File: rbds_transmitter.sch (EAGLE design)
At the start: 62 parts, among them IC1 MAX1551, IC2 TPS61030, IC3 MCP4812, IC4 OPA4743UA, Q1 P-Ch, SW1 FSMSM, U3 ATMEGA328, X1 HD44780LCD-1602, Y1 16Mhz

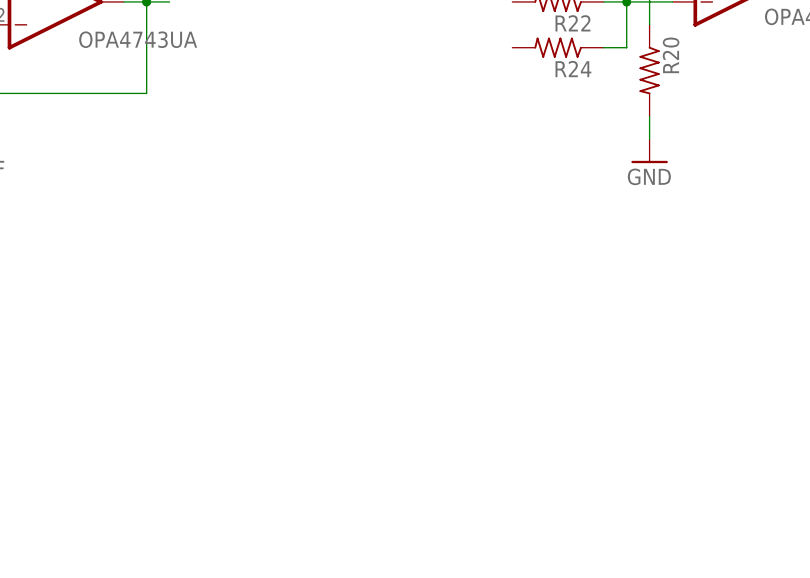
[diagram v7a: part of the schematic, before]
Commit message: adding low pass for pilot tones
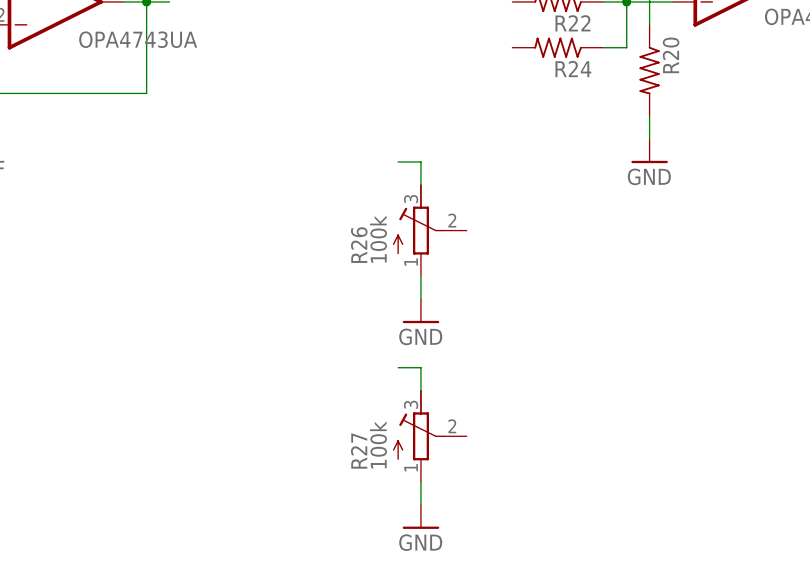
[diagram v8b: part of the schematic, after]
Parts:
- added R26, R27: 100k, rcl:R-TRIMM4G/J
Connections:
- new net N$32: R27.E
- new net N$33: R26.E
- net GND: now also R26.A, R27.A
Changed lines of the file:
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@@
 <part name="GND27" library="sparkfun" deviceset="GND" device=""/>
 <part name="C13" library="adafruit" deviceset="C-US" device="C1206" value="3.8nF"/>
+<part name="R26" library="rcl" deviceset="R-TRIMM" device="4G/J" value="100k"/>
+<part name="R27" library="rcl" deviceset="R-TRIMM" device="4G/J" value="100k"/>
+<part name="GND29" library="sparkfun" deviceset="GND" device=""/>
+<part name="GND30" library="sparkfun" deviceset="GND" device=""/>
 </parts>
 <sheets>
@@
 <instance part="GND27" gate="1" x="330.2" y="-60.96"/>
 <instance part="C13" gate="G$1" x="320.04" y="-22.86" rot="R90"/>
+<instance part="R26" gate="G$1" x="383.54" y="-58.42"/>
+<instance part="R27" gate="G$1" x="383.54" y="-81.28"/>
+<instance part="GND29" gate="1" x="383.54" y="-91.44"/>
+<instance part="GND30" gate="1" x="383.54" y="-68.58"/>
 </instances>
 <busses>
@@
 <pinref part="GND27" gate="1" pin="GND"/>
 <wire x1="330.2" y1="-58.42" x2="330.2" y2="-53.34" width="0.1524" layer="91"/>
+</segment>
+<segment>
+<pinref part="GND30" gate="1" pin="GND"/>
+<pinref part="R26" gate="G$1" pin="A"/>
+<wire x1="383.54" y1="-63.5" x2="383.54" y2="-66.04" width="0.1524" layer="91"/>
+</segment>
+<segment>
+<pinref part="GND29" gate="1" pin="GND"/>
+<pinref part="R27" gate="G$1" pin="A"/>
+<wire x1="383.54" y1="-86.36" x2="383.54" y2="-88.9" width="0.1524" layer="91"/>
 </segment>
 </net>
@@
 </segment>
 </net>
+<net name="N$32" class="0">
+<segment>
+<pinref part="R27" gate="G$1" pin="E"/>
+<wire x1="383.54" y1="-76.2" x2="383.54" y2="-73.66" width="0.1524" layer="91"/>
+<wire x1="383.54" y1="-73.66" x2="381" y2="-73.66" width="0.1524" layer="91"/>
+</segment>
+</net>
+<net name="N$33" class="0">
+<segment>
+<pinref part="R26" gate="G$1" pin="E"/>
+<wire x1="383.54" y1="-53.34" x2="383.54" y2="-50.8" width="0.1524" layer="91"/>
+<wire x1="383.54" y1="-50.8" x2="381" y2="-50.8" width="0.1524" layer="91"/>
+</segment>
+</net>
